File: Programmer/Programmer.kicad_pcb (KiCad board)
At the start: 2 copper layers, 41 x 20 mm, 17 parts, among them J1 USB_C_Receptacle_USB2.0, J2 Prog, Q1 BC846BS, U1 AP2112K-3.3, U2 FT232RL-REEL

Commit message: Rettelse på programmer vcc
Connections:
- C4 pad 1: Net-(C4-Pad1) -> VCC
- D1 pad 3: Net-(D1-Pad3) -> (no net)
- D1 pad 4: Net-(D1-Pad4) -> (no net)
- J1 pad A8: Net-(J1-PadA8) -> (no net)
- J1 pad B6: Net-(J1-PadB6) -> (no net)
- J1 pad B7: Net-(J1-PadB7) -> (no net)
- J1 pad B8: Net-(J1-PadB8) -> (no net)
- J1 pad S1: Net-(J1-PadS1) -> GNDD
- U1 pad 4: Net-(U1-Pad4) -> (no net)
- U2 pad 10: Net-(U2-Pad10) -> (no net)
- U2 pad 11: Net-(U2-Pad11) -> (no net)
- U2 pad 12: Net-(U2-Pad12) -> (no net)
- U2 pad 13: Net-(U2-Pad13) -> (no net)
- U2 pad 14: Net-(U2-Pad14) -> (no net)
- U2 pad 17: Net-(C4-Pad1) -> VCC
- U2 pad 19: Net-(U2-Pad19) -> VCC
- U2 pad 22: Net-(U2-Pad22) -> (no net)
- U2 pad 23: Net-(U2-Pad23) -> (no net)
- U2 pad 24: Net-(U2-Pad24) -> (no net)
- U2 pad 27: Net-(U2-Pad27) -> (no net)
- U2 pad 28: Net-(U2-Pad28) -> (no net)
- U2 pad 4: +3V3 -> VCC
- U2 pad 6: Net-(U2-Pad6) -> (no net)
- U2 pad 8: Net-(U2-Pad8) -> (no net)
- U2 pad 9: Net-(U2-Pad9) -> (no net)
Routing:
- net VCC: track 0.00 -> 16.8 mm, vias 0 -> 2
- net +3V3: track 30.6 -> 22.7 mm
- net Net-(C4-Pad1): track 2.51 -> 0.00 mm
- net GNDD: track 25.3 -> 26.1 mm, vias 9 -> 10
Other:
- board text added: "(c)Gert Lauritsen 20200803"

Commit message: knap tilføjet
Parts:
- added D2: LED, LED_SMD:LED_0805_2012Metric, F.Cu at (132.0, 87.3)
- added D3: LED, LED_SMD:LED_0805_2012Metric, F.Cu at (132.0, 85.2)
- added R7: 1k, Resistor_SMD:R_0805_2012Metric, F.Cu at (135.6, 87.3)
- added R8: 1k, Resistor_SMD:R_0805_2012Metric, F.Cu at (135.6, 85.2)
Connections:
- D1 pad 3: (no net) -> Net-(D1-Pad3)
- D1 pad 4: (no net) -> Net-(D1-Pad4)
- J1 pad A8: (no net) -> Net-(J1-PadA8)
- J1 pad B6: (no net) -> Net-(J1-PadB6)
- J1 pad B7: (no net) -> Net-(J1-PadB7)
- J1 pad B8: (no net) -> Net-(J1-PadB8)
- U1 pad 4: (no net) -> Net-(U1-Pad4)
- U2 pad 10: (no net) -> Net-(U2-Pad10)
- U2 pad 11: (no net) -> Net-(U2-Pad11)
- U2 pad 12: (no net) -> Net-(U2-Pad12)
- U2 pad 13: (no net) -> Net-(U2-Pad13)
- U2 pad 14: (no net) -> Net-(U2-Pad14)
- U2 pad 22: (no net) -> Net-(D2-Pad1)
- U2 pad 23: (no net) -> Net-(D3-Pad1)
- U2 pad 24: (no net) -> Net-(U2-Pad24)
- U2 pad 27: (no net) -> Net-(U2-Pad27)
- U2 pad 28: (no net) -> Net-(U2-Pad28)
- U2 pad 6: (no net) -> Net-(U2-Pad6)
- U2 pad 8: (no net) -> Net-(U2-Pad8)
- U2 pad 9: (no net) -> Net-(U2-Pad9)
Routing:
- net VCC: track 16.8 -> 30.2 mm
- net Net-(D2-Pad1): track 0.00 -> 5.08 mm
- net Net-(D3-Pad1): track 0.00 -> 2.62 mm
- net Net-(D3-Pad2): track 0.00 -> 1.72 mm
- net Net-(D2-Pad2): track 0.00 -> 1.72 mm
- net GNDD: track 26.1 -> 26.9 mm
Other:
- board size 41 x 20 mm -> 41 x 22 mm

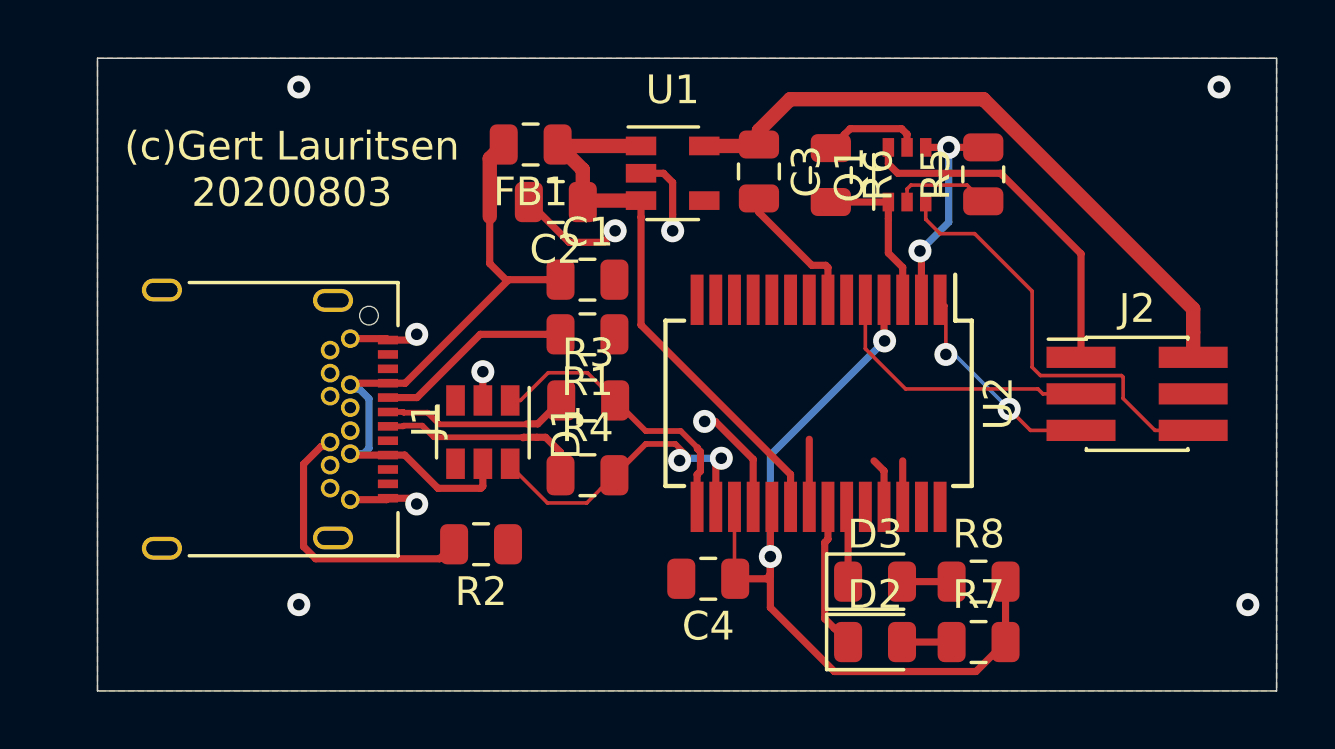
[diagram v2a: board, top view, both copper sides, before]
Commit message: Final edit
Ændret LDO , da jeg ikke kunne skaffe den anden på mouser kun i kina, hvilket jeg ikke har tid til. Rettet en bane der kom lidt for tæt og fejlede i første forsøg
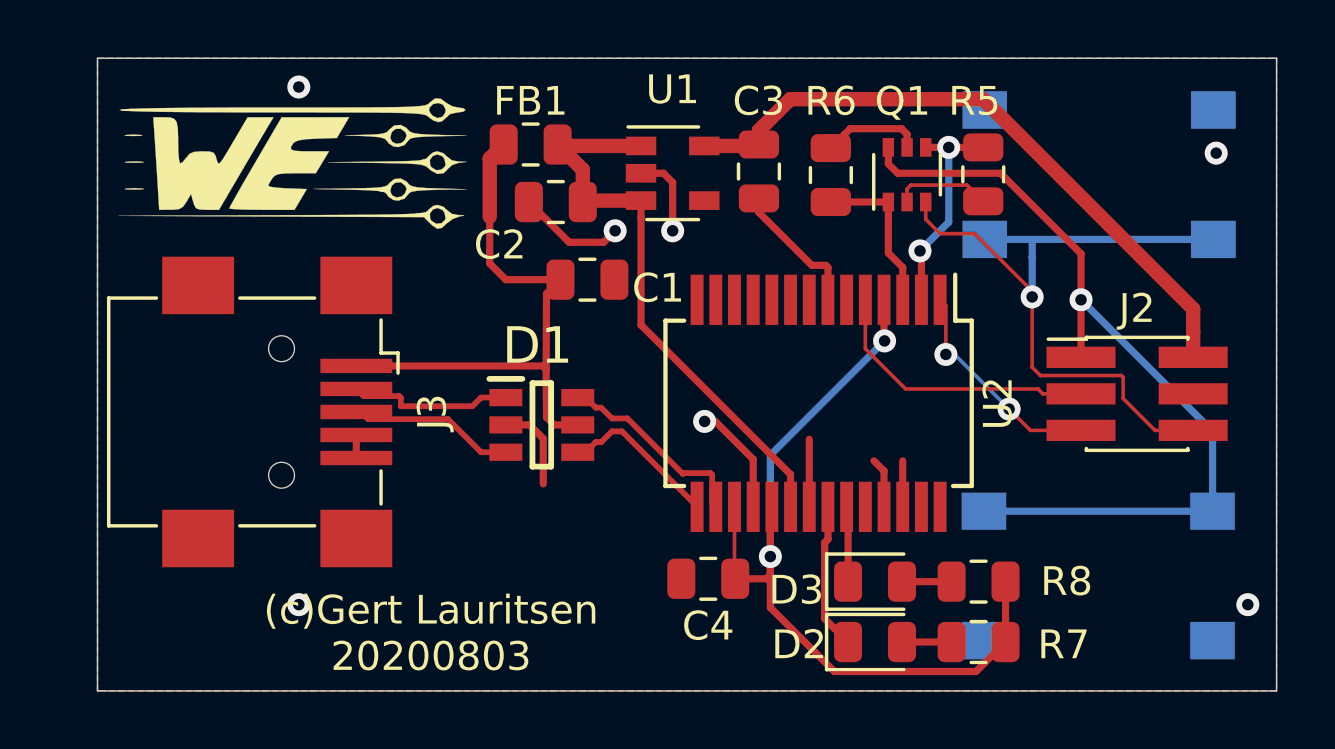
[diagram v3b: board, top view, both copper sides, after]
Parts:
- removed J1: USB_C_Receptacle_USB2.0, Connector_USB:USB_C_Receptacle_Amphenol_12401548E4-2A
- removed R1, R2, R3, R4: 5k1, Resistor_SMD:R_0805_2012Metric
- added G***: LOGO, IdaDemo:WE_Small, F.Cu at (111.7, 71.0)
- added J3: USB_A, Connector_USB:USB_Mini-B_Wuerth_65100516121_Horizontal, F.Cu at (111.4, 79.3)
- added SW1: SW_Push, Button_Switch_SMD:SW_Push_1P1T_NO_6x6mm_H9.5mm, B.Cu at (139.8, 85.0)
- added SW2: SW_Push, Button_Switch_SMD:SW_Push_1P1T_NO_6x6mm_H9.5mm, B.Cu at (139.8, 71.0)
- D1: value 824014 -> 82400102; footprint Package_TO_SOT_SMD:SOT-23-6 -> SamacSys_Parts:SOT95P280X145-6N
- moved D1 2.07 mm to (120.5, 79.8), turned to 0 degrees
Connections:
- D1 pad 1: D+ -> /D_N
- D1 pad 3: Net-(D1-Pad3) -> /D_P
- D1 pad 4: Net-(D1-Pad4) -> D+
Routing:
- net EN: track 12.2 -> 29.4 mm, vias 0 -> 1
- net D0: track 14.9 -> 24.9 mm, vias 0 -> 1
- net Net-(J1-PadB5): track 9.73 -> 0.00 mm
- net Net-(J1-PadA5): track 6.91 -> 0.00 mm
- net D+: track 10.1 -> 5.55 mm
- net D-: track 11.4 -> 6.98 mm, vias 2 -> 0
- net VBUS: track 23.5 -> 19.9 mm
- net GNDD: track 26.9 -> 24.9 mm, vias 10 -> 7
- net /D_N: track 7.40 -> 5.74 mm
- net /D_P: track 6.67 -> 5.78 mm
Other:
- board text added: "D0"
- board text added: "Enable"
